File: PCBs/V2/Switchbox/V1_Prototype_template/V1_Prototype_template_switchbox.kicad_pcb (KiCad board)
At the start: 2 copper layers, 70 x 35 mm, 9 parts, among them J3(IN)1 01x04 magnetic connector, J5(OUT)1 01x04 magnetic connector

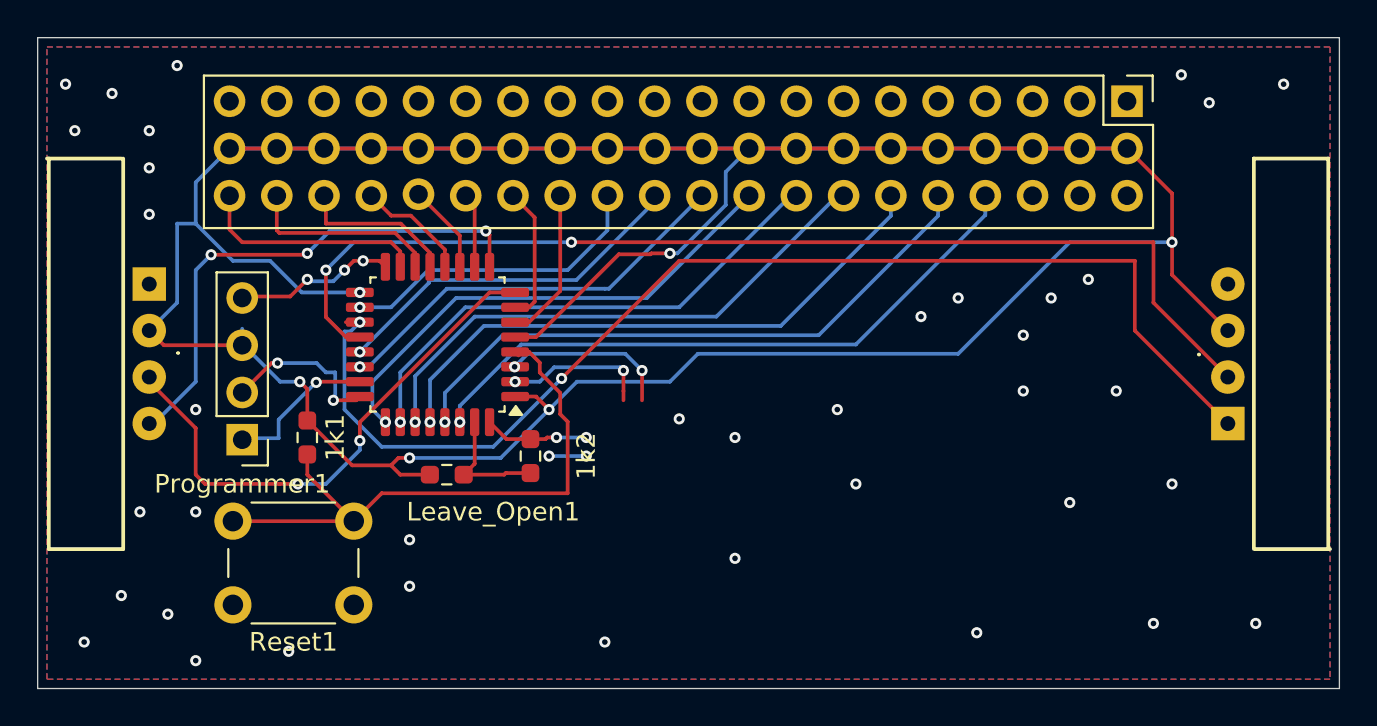
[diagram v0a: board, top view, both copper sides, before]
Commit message: testing and fixing PCBs, reordered
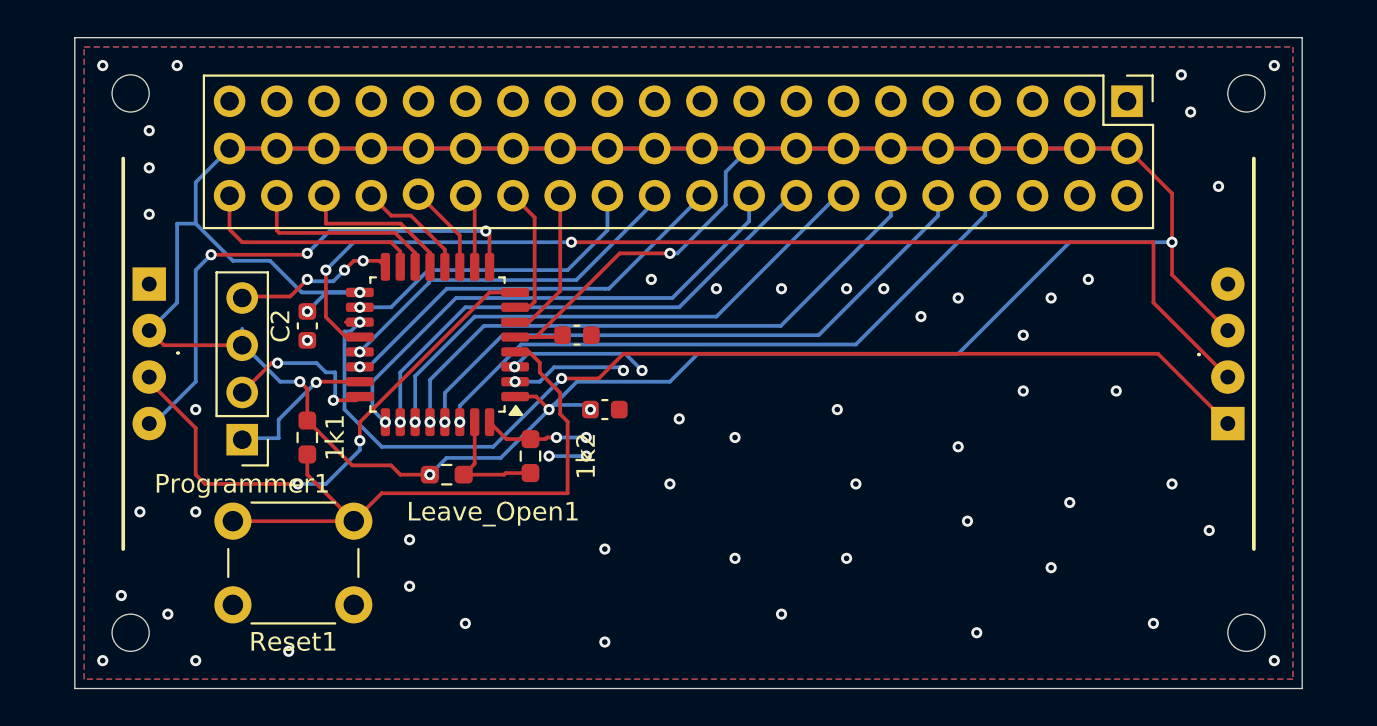
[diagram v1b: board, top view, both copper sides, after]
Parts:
- added C1: C, Capacitor_SMD:C_0603_1608Metric, F.Cu at (101.0, 75.0)
- added C2: C, Capacitor_SMD:C_0603_1608Metric, F.Cu at (86.5, 74.5)
- added C3: C, Capacitor_SMD:C_0603_1608Metric, F.Cu at (102.5, 79.0)
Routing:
- net /VCC: track 218.4 -> 224.8 mm, vias 6 -> 8
- net /NEXT_USART2_TX(PA9): track 64.3 -> 57.9 mm
- net /PC14: track 7.82 -> 6.22 mm
- net /PC15: track 9.14 -> 7.54 mm
- net /PA15: track 26.9 -> 27.7 mm
- net /GND: vias 45 -> 59
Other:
- board size 70 x 35 mm -> 66 x 35 mm
